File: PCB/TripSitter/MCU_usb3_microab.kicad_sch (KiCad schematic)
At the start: 9 parts, among them IC4 IP4220CZ6, J8 USB3_B_Micro

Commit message: before
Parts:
- removed TP2: DP_Probe, TestPoint:TestPoint_Pad_2.5x2.5mm, symbol Connector:TestPoint
- removed TP3: DM_Probe, TestPoint:TestPoint_Pad_2.5x2.5mm, symbol Connector:TestPoint
- renumbered IC4 to IC701, J8 to J701
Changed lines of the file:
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@@
   (junction (at 139.7 81.28) (diameter 0) (color 0 0 0 0)
   )
+  (junction (at 119.38 81.28) (diameter 0) (color 0 0 0 0)
+  )
   (junction (at 124.46 91.44) (diameter 0) (color 0 0 0 0)
   )
   (junction (at 151.13 86.36) (diameter 0) (color 0 0 0 0)
   )
-  (junction (at 129.54 88.9) (diameter 0) (color 0 0 0 0)
-  )
   (junction (at 153.67 88.9) (diameter 0) (color 0 0 0 0)
-  )
-  (junction (at 134.62 86.36) (diameter 0) (color 0 0 0 0)
   )
   (junction (at 121.92 91.44) (diameter 0) (color 0 0 0 0)
@@
     (stroke (width 0) (type default))
   )
-  (wire (pts (xy 109.22 81.28) (xy 139.7 81.28))
-    (stroke (width 0) (type default))
-  )
-  (wire (pts (xy 129.54 68.58) (xy 129.54 88.9))
+  (wire (pts (xy 109.22 81.28) (xy 119.38 81.28))
     (stroke (width 0) (type default))
   )
@@
     (stroke (width 0) (type default))
   )
-  (wire (pts (xy 134.62 68.58) (xy 134.62 86.36))
-    (stroke (width 0) (type default))
-  )
   (wire (pts (xy 172.72 76.2) (xy 184.15 76.2))
     (stroke (width 0) (type default))
@@
     (stroke (width 0) (type default))
   )
-  (wire (pts (xy 109.22 88.9) (xy 129.54 88.9))
-    (stroke (width 0) (type default))
-  )
   (wire (pts (xy 161.29 102.87) (xy 152.4 102.87))
     (stroke (width 0) (type default))
@@
     (stroke (width 0) (type default))
   )
-  (wire (pts (xy 129.54 88.9) (xy 153.67 88.9))
+  (wire (pts (xy 119.38 76.2) (xy 119.38 81.28))
+    (stroke (width 0) (type default))
+  )
+  (wire (pts (xy 109.22 88.9) (xy 153.67 88.9))
+    (stroke (width 0) (type default))
+  )
+  (wire (pts (xy 119.38 81.28) (xy 139.7 81.28))
     (stroke (width 0) (type default))
   )
@@
     (stroke (width 0) (type default))
   )
-  (wire (pts (xy 134.62 86.36) (xy 151.13 86.36))
+  (wire (pts (xy 109.22 86.36) (xy 151.13 86.36))
     (stroke (width 0) (type default))
   )
@@
   )
   (wire (pts (xy 121.92 91.44) (xy 124.46 91.44))
-    (stroke (width 0) (type default))
-  )
-  (wire (pts (xy 109.22 86.36) (xy 134.62 86.36))
     (stroke (width 0) (type default))
   )
@@
         (path "/e9047d94-28be-4266-894b-6ee25ef088bd/f9a74965-bde5-47a2-9f66-243cb6fc0f53/f8dfcd07-d713-410a-88b5-31ae3a6c85dd"
           (reference "R1102") (unit 1)
-        )
-      )
-    )
-  )
-  (symbol (lib_id "Connector:TestPoint") (at 129.54 68.58 0) (unit 1)
-    (in_bom yes) (on_board yes) (dnp no)
-    (property "Reference" "TP2" (at 129.54 63.5 90)
-      (effects (font (size 1.27 1.27)) (justify left))
-    )
-    (property "Value" "DP_Probe" (at 132.08 63.5 90)
-      (effects (font (size 1.27 1.27)) (justify left))
-    )
-    (property "Footprint" "TestPoint:TestPoint_Pad_2.5x2.5mm" (at 134.62 68.58 0)
-      (effects (font (size 1.27 1.27)) hide)
-    )
-    (property "Datasheet" "~" (at 134.62 68.58 0)
-      (effects (font (size 1.27 1.27)) hide)
-    )
-    (pin "1")
-    (instances
-      (project "TripSitter"
-        (path "/5ab65702-9689-4dfd-8f10-6407062323a6/87bcf595-d251-4aa5-8b35-efc055826b19/750eb09f-8f96-43e9-bfb8-1e6e7cd9bea9"
-          (reference "TP2") (unit 1)
-        )
-      )
-      (project "USB3_micro_ab"
-        (path "/aa8c6d6c-263c-4a63-9451-4860d8f398eb"
-          (reference "TP11") (unit 1)
-        )
-      )
-      (project "RayTracingPCB"
-        (path "/e9047d94-28be-4266-894b-6ee25ef088bd/f9a74965-bde5-47a2-9f66-243cb6fc0f53"
-          (reference "TP11") (unit 1)
-        )
-        (path "/e9047d94-28be-4266-894b-6ee25ef088bd/f9a74965-bde5-47a2-9f66-243cb6fc0f53/f8dfcd07-d713-410a-88b5-31ae3a6c85dd"
-          (reference "TPJ1105") (unit 1)
         )
       )
@@
     )
   )
-  (symbol (lib_id "Connector:TestPoint") (at 134.62 68.58 0) (unit 1)
-    (in_bom yes) (on_board yes) (dnp no)
-    (property "Reference" "TP3" (at 134.62 63.5 90)
-      (effects (font (size 1.27 1.27)) (justify left))
-    )
-    (property "Value" "DM_Probe" (at 137.16 63.5 90)
-      (effects (font (size 1.27 1.27)) (justify left))
-    )
-    (property "Footprint" "TestPoint:TestPoint_Pad_2.5x2.5mm" (at 139.7 68.58 0)
-      (effects (font (size 1.27 1.27)) hide)
-    )
-    (property "Datasheet" "~" (at 139.7 68.58 0)
-      (effects (font (size 1.27 1.27)) hide)
-    )
-    (pin "1")
-    (instances
-      (project "TripSitter"
-        (path "/5ab65702-9689-4dfd-8f10-6407062323a6/87bcf595-d251-4aa5-8b35-efc055826b19/750eb09f-8f96-43e9-bfb8-1e6e7cd9bea9"
-          (reference "TP3") (unit 1)
-        )
-      )
-      (project "USB3_micro_ab"
-        (path "/aa8c6d6c-263c-4a63-9451-4860d8f398eb"
-          (reference "TP11") (unit 1)
-        )
-      )
-      (project "RayTracingPCB"
-        (path "/e9047d94-28be-4266-894b-6ee25ef088bd/f9a74965-bde5-47a2-9f66-243cb6fc0f53"
-          (reference "TP11") (unit 1)
-        )
-        (path "/e9047d94-28be-4266-894b-6ee25ef088bd/f9a74965-bde5-47a2-9f66-243cb6fc0f53/f8dfcd07-d713-410a-88b5-31ae3a6c85dd"
-          (reference "TPJ1106") (unit 1)
+  (symbol (lib_id "power:VBUS") (at 119.38 76.2 0) (unit 1)
+    (in_bom yes) (on_board yes) (dnp no) (fields_autoplaced)
+    (property "Reference" "#PWR047" (at 119.38 80.01 0)
+      (effects (font (size 1.27 1.27)) hide)
+    )
+    (property "Value" "VBUS" (at 119.38 71.12 0)
+      (effects (font (size 1.27 1.27)))
+    )
+    (property "Footprint" "" (at 119.38 76.2 0)
+      (effects (font (size 1.27 1.27)) hide)
+    )
+    (property "Datasheet" "" (at 119.38 76.2 0)
+      (effects (font (size 1.27 1.27)) hide)
+    )
+    (pin "1")
+    (instances
+      (project "TripSitter"
+        (path "/5ab65702-9689-4dfd-8f10-6407062323a6/87bcf595-d251-4aa5-8b35-efc055826b19/750eb09f-8f96-43e9-bfb8-1e6e7cd9bea9"
+          (reference "#PWR047") (unit 1)
         )
       )
@@
   (symbol (lib_id "IP4220CZ6:IP4220CZ6") (at 129.54 107.95 0) (unit 1)
     (in_bom yes) (on_board yes) (dnp no)
-    (property "Reference" "IC4" (at 144.78 100.33 0)
+    (property "Reference" "IC701" (at 144.78 100.33 0)
       (effects (font (size 1.27 1.27)))
     )
@@
       (project "TripSitter"
         (path "/5ab65702-9689-4dfd-8f10-6407062323a6/87bcf595-d251-4aa5-8b35-efc055826b19/750eb09f-8f96-43e9-bfb8-1e6e7cd9bea9"
-          (reference "IC4") (unit 1)
+          (reference "IC701") (unit 1)
         )
         (path "/5ab65702-9689-4dfd-8f10-6407062323a6/8ae76c2e-e928-4bfb-9cc2-9dfcb5e6a658"
@@
   (symbol (lib_id "Connector:USB3_B_Micro") (at 96.52 91.44 0) (unit 1)
     (in_bom yes) (on_board yes) (dnp no) (fields_autoplaced)
-    (property "Reference" "J8" (at 96.52 72.39 0)
+    (property "Reference" "J701" (at 96.52 72.39 0)
       (effects (font (size 1.27 1.27)))
     )
@@
       (project "TripSitter"
         (path "/5ab65702-9689-4dfd-8f10-6407062323a6/87bcf595-d251-4aa5-8b35-efc055826b19/750eb09f-8f96-43e9-bfb8-1e6e7cd9bea9"
-          (reference "J8") (unit 1)
-        )
-      )
+          (reference "J701") (unit 1)
+        )
+      )

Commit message: more pcb routing
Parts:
- removed J701: USB3_B_Micro, Connector_USB:USB_Micro-B_Wuerth_629105150521_CircularHoles, symbol Connector:USB3_B_Micro
- added J3: USB_B_Micro, Connector_USB:USB_Micro-B_GCT_USB3076-30-A, symbol Connector:USB_B_Micro
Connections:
- net D+: now also J3.2 (D-)
- net D-: now also J3.3 (D+)
- net EFM32GG11_USB_ID: now also J3.4 (ID)
- net GND: now also J3.5 (GND), J3.6 (Shield)
- net VBUS: now also J3.1 (VBUS)
- net EFM32GG11_USB_DM renamed EFM32GG11_USB_D-
- net EFM32GG11_USB_DP renamed EFM32GG11_USB_D+
- no-connect marks 6 -> 1

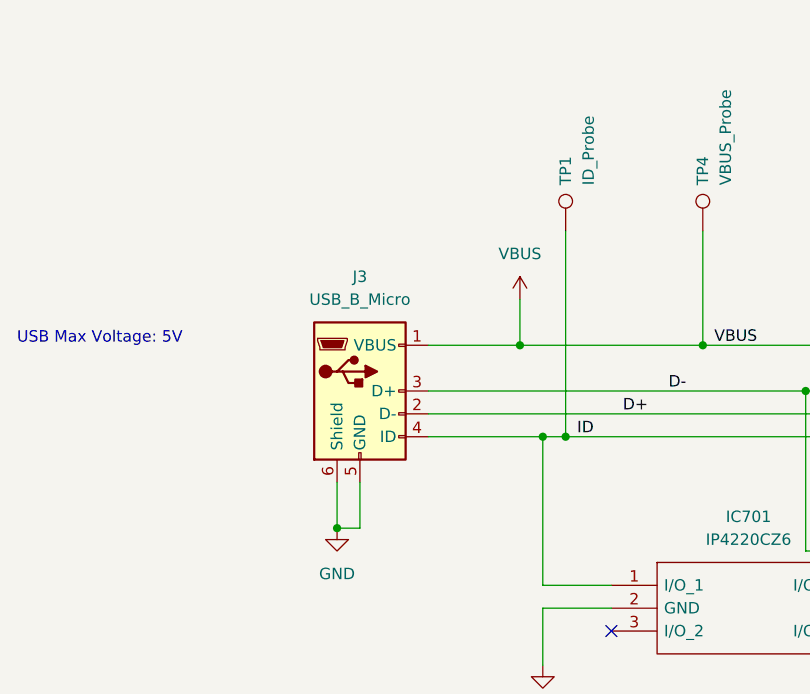
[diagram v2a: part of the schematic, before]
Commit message: pcb: Finalized routing without DDR3
Added ground and power plane, layed out all the components, fanned out
BGA. QSPI between FPGA->MCU->SRAM and MCU->SRAM is routed. Most is done
but DRC does not pass so do not produce.
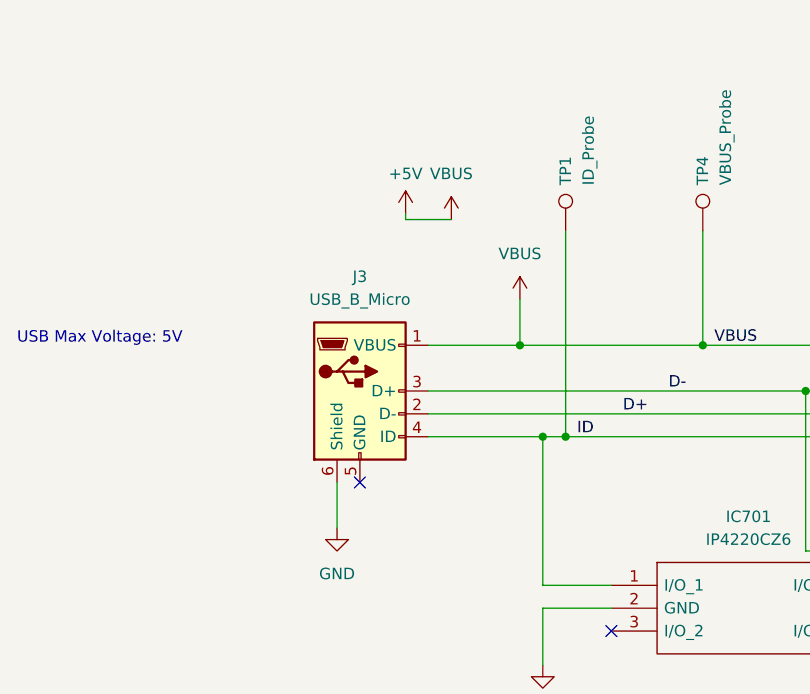
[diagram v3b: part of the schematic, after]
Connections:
- net GND: no longer J3.5 (GND)
- net VBUS renamed +5V
- no-connect marks 1 -> 2
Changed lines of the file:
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@@
   (junction (at 151.13 86.36) (diameter 0) (color 0 0 0 0)
   )
-  (junction (at 99.06 101.6) (diameter 0) (color 0 0 0 0)
-  )
   (junction (at 153.67 88.9) (diameter 0) (color 0 0 0 0)
   )
@@
   (junction (at 177.8 86.36) (diameter 0) (color 0 0 0 0)
   )
+  (no_connect (at 101.6 96.52))
   (no_connect (at 129.54 113.03))
   (wire (pts (xy 161.29 110.49) (xy 161.29 102.87))
     (stroke (width 0) (type default))
   )
-  (wire (pts (xy 99.06 101.6) (xy 101.6 101.6))
-    (stroke (width 0) (type default))
-  )
   (wire (pts (xy 172.72 88.9) (xy 177.8 88.9))
     (stroke (width 0) (type default))
@@
     (stroke (width 0) (type default))
   )
+  (wire (pts (xy 106.68 66.675) (xy 106.68 67.31))
+    (stroke (width 0) (type default))
+  )
   (wire (pts (xy 109.22 81.28) (xy 119.38 81.28))
     (stroke (width 0) (type default))
@@
     (stroke (width 0) (type default))
   )
-  (wire (pts (xy 101.6 101.6) (xy 101.6 96.52))
-    (stroke (width 0) (type default))
-  )
   (wire (pts (xy 162.56 113.03) (xy 162.56 101.6))
     (stroke (width 0) (type default))
@@
     (stroke (width 0) (type default))
   )
+  (wire (pts (xy 99.06 96.52) (xy 99.06 101.6))
+    (stroke (width 0) (type default))
+  )
   (wire (pts (xy 153.67 88.9) (xy 153.67 101.6))
     (stroke (width 0) (type default))
@@
     (stroke (width 0) (type default))
   )
+  (wire (pts (xy 106.68 67.31) (xy 111.76 67.31))
+    (stroke (width 0) (type default))
+  )
   (wire (pts (xy 109.22 86.36) (xy 151.13 86.36))
     (stroke (width 0) (type default))
@@
   )
   (wire (pts (xy 139.7 81.28) (xy 152.4 81.28))
-    (stroke (width 0) (type default))
-  )
-  (wire (pts (xy 99.06 101.6) (xy 99.06 96.52))
     (stroke (width 0) (type default))
   )
@@
         )
       )
+    )
+  )
+  (symbol (lib_id "power:+5V") (at 106.68 66.675 0) (mirror y) (unit 1)
+    (in_bom yes) (on_board yes) (dnp no)
+    (property "Reference" "#PWR030" (at 106.68 70.485 0)
+      (effects (font (size 1.27 1.27)) hide)
+    )
+    (property "Value" "+5V" (at 106.68 62.23 0)
+      (effects (font (size 1.27 1.27)))
+    )
+    (property "Footprint" "" (at 106.68 66.675 0)
+      (effects (font (size 1.27 1.27)) hide)
+    )
+    (property "Datasheet" "" (at 106.68 66.675 0)
+      (effects (font (size 1.27 1.27)) hide)
+    )
+    (pin "1")
+    (instances
+      (project "TripSitter"
+        (path "/5ab65702-9689-4dfd-8f10-6407062323a6/87bcf595-d251-4aa5-8b35-efc055826b19/750eb09f-8f96-43e9-bfb8-1e6e7cd9bea9"
+          (reference "#PWR030") (unit 1)
+        )
+      )
+    )
+  )
+  (symbol (lib_id "power:VBUS") (at 111.76 67.31 0) (mirror y) (unit 1)
+    (in_bom yes) (on_board yes) (dnp no)
+    (property "Reference" "#PWR029" (at 111.76 71.12 0)
+      (effects (font (size 1.27 1.27)) hide)
+    )
+    (property "Value" "VBUS" (at 111.76 62.23 0)
+      (effects (font (size 1.27 1.27)))
+    )
+    (property "Footprint" "" (at 111.76 67.31 0)
+      (effects (font (size 1.27 1.27)) hide)
+    )
+    (property "Datasheet" "" (at 111.76 67.31 0)
+      (effects (font (size 1.27 1.27)) hide)
+    )
+    (pin "1")
+    (instances
+      (project "TripSitter"
+        (path "/5ab65702-9689-4dfd-8f10-6407062323a6/87bcf595-d251-4aa5-8b35-efc055826b19/750eb09f-8f96-43e9-bfb8-1e6e7cd9bea9"
+          (reference "#PWR029") (unit 1)
+        )
+      )
